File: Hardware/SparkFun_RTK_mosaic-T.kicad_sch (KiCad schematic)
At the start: 23 parts, among them J3 Qwiic_RA, U1 ESP32-WROVER-IE-N16R8

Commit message: More WIP
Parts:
- removed J3: Qwiic_RA, SparkFun-Connector:JST_SMD_1.0mm-4_RA, symbol SparkFun-Connector:Qwiic_Right_Angle
- added J7: Qwiic_Vertical, SparkFun-Connector:JST_SMD_1.0mm-4_Vertical, symbol SparkFun-Connector:Qwiic_Vertical
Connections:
- net 3.3V: now also J7.2 (Pin_2)
- net ESP21/SDA: now also J7.3 (Pin_3)
- net ESP22/SCL: now also J7.4 (Pin_4)
- net GND: now also J7.1 (Pin_1)
- new net: J7.NC1 (NC), J7.NC2 (NC)
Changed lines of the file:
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@@
+	)
+	(symbol
+		(lib_id "SparkFun-PowerSymbol:3.3V")
+		(at 222.25 36.83 0)
+		(unit 1)
+		(exclude_from_sim no)
+		(in_bom yes)
+		(on_board yes)
+		(dnp no)
+		(property "Reference" "#PWR0101"
+			(at 222.25 40.64 0)
+			(effects
+				(font
+					(size 1.27 1.27)
+				)
+				(hide yes)
+			)
+		)
+		(property "Value" "3.3V"
+			(at 222.25 33.274 0)
+			(effects
+				(font
+					(size 1.27 1.27)
+				)
+			)
+		)
+		(property "Footprint" ""
+			(at 222.25 36.83 0)
+			(effects
+				(font
+					(size 1.27 1.27)
+				)
+				(hide yes)
+			)
+		)
+		(property "Datasheet" ""
+			(at 222.25 36.83 0)
+			(effects
+				(font
+					(size 1.27 1.27)
+				)
+				(hide yes)
+			)
+		)
+		(property "Description" "Power symbol creates a global label with name \"3.3V\""
+			(at 222.25 36.83 0)
+			(effects
+				(font
+					(size 1.27 1.27)
+				)
+				(hide yes)
+			)
+		)
+		(pin "1"
+		)
+		(instances
+			(project "SparkFun_RTK_mosaic-T"
+				(path "/e3dd3ae4-244d-4cba-9cca-5d2abf83f29a"
+					(reference "#PWR0101")
+					(unit 1)
+				)
+			)
+		)
 	)
 	(symbol
@@
 	)
 	(symbol
-		(lib_id "SparkFun-Connector:Qwiic_Right_Angle")
-		(at 228.6 40.64 0)
-		(unit 1)
-		(exclude_from_sim no)
-		(in_bom yes)
-		(on_board yes)
-		(dnp no)
-		(fields_autoplaced yes)
-		(property "Reference" "J3"
-			(at 237.49 40.64 0)
-			(effects
-				(font
-					(size 1.27 1.27)
-				)
-				(justify left)
-			)
-		)
-		(property "Value" "Qwiic_RA"
-			(at 237.49 43.18 0)
-			(effects
-				(font
-					(size 1.27 1.27)
-				)
-				(justify left)
-			)
-		)
-		(property "Footprint" "SparkFun-Connector:JST_SMD_1.0mm-4_RA"
-			(at 228.6 53.34 0)
-			(effects
-				(font
-					(size 1.27 1.27)
-				)
-				(hide yes)
-			)
-		)
-		(property "Datasheet" "https://www.jst-mfg.com/product/pdf/eng/eSH.pdf"
-			(at 228.6 55.88 0)
-			(effects
-				(font
-					(size 1.27 1.27)
-				)
-				(hide yes)
-			)
-		)
-		(property "Description" "4 pin JST 1mm polarized connector for I2C"
-			(at 228.6 40.64 0)
-			(effects
-				(font
-					(size 1.27 1.27)
-				)
-				(hide yes)
-			)
-		)
-		(property "PROD_ID" "CONN-13694"
-			(at 228.6 50.8 0)
-			(effects
-				(font
-					(size 1.27 1.27)
-				)
-				(hide yes)
-			)
-		)
-		(pin "1"
-		)
-		(pin "2"
-		)
-		(pin "3"
-		)
-		(pin "4"
-		)
-		(pin "NC1"
-		)
-		(pin "NC2"
-		)
-		(instances
-			(project "SparkFun_RTK_Facet_mosaic"
-				(path "/e3dd3ae4-244d-4cba-9cca-5d2abf83f29a"
-					(reference "J3")
-					(unit 1)
-				)
-			)
-		)
-	)
-	(symbol
 		(lib_id "SparkFun-Aesthetic:SparkFun_Logo")
 		(at 213.36 182.88 0)
@@
 	)
 	(symbol
+		(lib_id "SparkFun-Connector:Qwiic_Vertical")
+		(at 228.6 40.64 0)
+		(unit 1)
+		(exclude_from_sim no)
+		(in_bom yes)
+		(on_board yes)
+		(dnp no)
+		(fields_autoplaced yes)
+		(property "Reference" "J7"
+			(at 237.49 40.6399 0)
+			(effects
+				(font
+					(size 1.27 1.27)
+				)
+				(justify left)
+			)
+		)
+		(property "Value" "Qwiic_Vertical"
+			(at 237.49 43.1799 0)
+			(effects
+				(font
+					(size 1.27 1.27)
+				)
+				(justify left)
+			)
+		)
+		(property "Footprint" "SparkFun-Connector:JST_SMD_1.0mm-4_Vertical"
+			(at 228.6 53.34 0)
+			(effects
+				(font
+					(size 1.27 1.27)
+				)
+				(hide yes)
+			)
+		)
+		(property "Datasheet" "https://www.jst-mfg.com/product/pdf/eng/eSH.pdf"
+			(at 228.6 55.88 0)
+			(effects
+				(font
+					(size 1.27 1.27)
+				)
+				(hide yes)
+			)
+		)
+		(property "Description" "4 pin JST 1mm polarized connector for I2C"
+			(at 228.6 40.64 0)
+			(effects
+				(font
+					(size 1.27 1.27)
+				)
+				(hide yes)
+			)
+		)
+		(property "PROD_ID" "CONN-14483"
+			(at 228.6 50.8 0)
+			(effects
+				(font
+					(size 1.27 1.27)
+				)
+				(hide yes)
+			)
+		)
+		(pin "3"
+		)
+		(pin "2"
+		)
+		(pin "4"
+		)
+		(pin "NC2"
+		)
+		(pin "NC1"
+		)
+		(pin "1"
+		)
+		(instances
+			(project ""
+				(path "/e3dd3ae4-244d-4cba-9cca-5d2abf83f29a"
+					(reference "J7")
+					(unit 1)
+				)
+			)
+		)
+	)
+	(symbol
 		(lib_id "SparkFun-PowerSymbol:3.3V")
 		(at 55.88 106.68 0)
@@
 					(unit 1)
 				)
-			)
-		)
-	)
-	(symbol
-		(lib_id "SparkFun-PowerSymbol:3.3V_P")
-		(at 222.25 36.83 0)
-		(unit 1)
-		(exclude_from_sim no)
-		(in_bom yes)
-		(on_board yes)
-		(dnp no)
-		(property "Reference" "#PWR0101"
-			(at 222.25 40.64 0)
-			(effects
-				(font
-					(size 1.27 1.27)
-				)
-				(hide yes)
-			)
-		)
-		(property "Value" "3.3V_P"
-			(at 222.25 33.274 0)
-			(effects
-				(font
-					(size 1.27 1.27)
-				)
-			)
-		)
-		(property "Footprint" ""
-			(at 222.25 36.83 0)
-			(effects
-				(font
-					(size 1.27 1.27)
-				)
-				(hide yes)
-			)
-		)
-		(property "Datasheet" ""
-			(at 222.25 36.83 0)
-			(effects
-				(font
-					(size 1.27 1.27)
-				)
-				(hide yes)
-			)
-		)
-		(property "Description" "Power symbol creates a global label with name \"3.3V_P\""
-			(at 222.25 36.83 0)
-			(effects
-				(font
-					(size 1.27 1.27)
-				)
-				(hide yes)
-			)
-		)
-		(pin "1"
-		)
-		(instances
-			(project "SparkFun_RTK_Facet_mosaic"
-				(path "/e3dd3ae4-244d-4cba-9cca-5d2abf83f29a"
-					(reference "#PWR0101")
-					(unit 1)
-				)

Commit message: More WIP
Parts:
- added D11, D12: CBI_LED_3mm_YGR, SparkFun-LED:CBI_LED_Triple_3mm_PTH, symbol SparkFun-LED:CBI_LED_Triple_3mm_PTH_YGR
- added D15: PESD0402, SparkFun-Capacitor:C_0402_1005Metric, symbol SparkFun-DiscreteSemi:D_TVS_0402
- added J3: U.FL, SparkFun-Connector:U.FL, symbol SparkFun-RF:U.FL
- added J8: RP-SMA_Edge, SparkFun-Connector:RP-SMA_Edge, symbol SparkFun-RF:RP-SMA_EdgeMount
- added J9: Screw_Cage_3.5mm-10, SparkFun-Connector:Screw_Cage_3.5mm-10, symbol SparkFun-Connector:Screw_Cage_3.5mm-10
- added R12, R13, R38, R39, R40, R42: 470, SparkFun-Resistor:R_0603_1608Metric, symbol SparkFun-Resistor:470_0603
- FID1, FID2, FID3, FID4: value Fiducial_0.5 -> Fiducial_0.5mm
- G5: footprint SparkFun-Aesthetic:SparkFun_Logo_8mm -> (none)
- renumbered TP5 to TP1
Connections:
- net 3.3V: now also R38.2
- net GND: now also D11.CATHODE_1, D11.CATHODE_2, D11.CATHODE_3, D12.CATHODE_1, D12.CATHODE_2, D12.CATHODE_3, D15.1 (A1), J3.2 (Ext), J8.2 (Ext), J9.8 (Pin_1)
- net ESP26/MCTS1: now reaches U1.11 (IOA26)
- net ESP27/MRTS1: now reaches U1.12 (IOA27)
- net ESP32/LED_ERROR: now reaches U1.8 (IOA32)
- net ESP32/LED_ERROR: now also R12.2
- net ESP33/LED_LOCK: now reaches U1.9 (IOA33)
- net ESP33/LED_LOCK: now also R13.2
- net ESP~{RST} renamed ESP_~{RST}
- new net: D11.ANODE_3, R38.1
- new net: D12.ANODE_1, R39.1
- new net: D12.ANODE_2, R40.1
- new net: D12.ANODE_3, R42.1
- new net: D11.ANODE_1, R12.1
- new net: D11.ANODE_2, R13.1
- new net 50Ohm: D15.2 (A2), J3.1 (In), J8.1 (In)
- new net DC_IN+: J9.10 (Pin_1)
- new net DC_IN-: J9.9 (Pin_1)
- new net LED_LOG: R42.2
- new net LED_PVT: R40.2
- new net LED_RTK: R39.2
- new net MCTS2_I: J9.7 (Pin_2)
- new net MEventA_I: J9.3 (Pin_3)
- new net MEventB_I: J9.2 (Pin_2)
- new net MPPS_O: J9.1 (Pin_1)
- new net MRTS2_O: J9.6 (Pin_4)
- new net MRX2_I: J9.4 (Pin_4)
- new net MTX2_O: J9.5 (Pin_3)
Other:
- added sheet Level_Shifting (Level_Shifting.kicad_sch)
- added sheet Oscillator (Oscillator.kicad_sch)
- note added: "ESP32 RF"
- note added: "I/O Connector"
- note added: "LEDs"
- note removed: "Connectors"

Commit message: More WIP
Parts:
- added TP24: PTH, SparkFun-Connector:1x01, symbol SparkFun-Connector:TestPoint_PTH
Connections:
- net ESP35/DeviceSense: now also TP24.1
- net ESP18/SDA2: now reaches U1.30 (IO18)
- net ESP19/SCL2: now reaches U1.31 (IO19)
- net 50Ohm: no longer names the net of D15.2 (A2), J3.1 (In), J8.1 (In)
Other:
- removed sheet Oscillator
- note added: "50Ohm"
- note added: "Qwiic I²C (for OLED)"
- note removed: "Qwiic I²C"
- moved on the sheet: D11, D12, D15, J3, J8, J9, R12, R13, R38, R39, R40, R42

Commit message: Schematic complete
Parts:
- removed R8: 4.7k, SparkFun-Resistor:R_0402_1005Metric, symbol SparkFun-Resistor:4.7k_0402
- added C53: 10uF, SparkFun-Capacitor:C_0402_1005Metric, symbol SparkFun-Capacitor:10uF_0402_6.3V_20%
- added C54: 0.1uF, SparkFun-Capacitor:C_0603_1608Metric, symbol SparkFun-Capacitor:0.1uF_0603_25V_20%
- added JP15: ~, SparkFun-Jumper:Jumper_2_NO, symbol SparkFun-Jumper:SolderJumper_2_Open
- added JP16, JP17, JP18, JP19, JP20, JP21: ~, SparkFun-Jumper:Jumper_2_NC_Trace, symbol SparkFun-Jumper:SolderJumper_2_Bridged
- added R8: 1k, SparkFun-Resistor:R_0402_1005Metric, symbol SparkFun-Resistor:1k_0402
- added TP25, TP26, TP41, TP42, TP43: PTH, SparkFun-Connector:1x01, symbol SparkFun-Connector:TestPoint_PTH
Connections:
- net ESP21/SDA: now also TP26.1
- net ESP22/SCL: now also TP25.1
- net ESP35/DeviceSense: now also R8.1
- net GND: now also C53.2, C54.2, R8.2
- net MCTS2_I: now also J9.4 (Pin_4), JP15.1 (A); no longer J9.7 (Pin_2)
- net MRTS2_O: now also J9.5 (Pin_3); no longer J9.6 (Pin_4)
- net MRX2_I: now also J9.7 (Pin_2); no longer J9.4 (Pin_4)
- net MTX2_O: now also J9.6 (Pin_4); no longer J9.5 (Pin_3)
- net at R38.1: now also JP18.1 (A); no longer D11.ANODE_3
- net at U1.37 (IO23): now also TP41.1
- net at U1.5 (IA39): now also TP43.1
- net at U1.6 (IA34): now also TP42.1
- net at R39.1: now also JP19.1 (A); no longer D12.ANODE_1
- net at R40.1: now also JP20.1 (A); no longer D12.ANODE_2
- net at D12.ANODE_3: now also JP21.2 (B); no longer R42.1
- net at R12.1: now also JP16.1 (A); no longer D11.ANODE_1
- net at R13.1: now also JP17.1 (A); no longer D11.ANODE_2
- new net: D12.ANODE_2, JP20.2 (B)
- new net: D12.ANODE_1, JP19.2 (B)
- new net: D11.ANODE_2, JP17.2 (B)
- new net: D11.ANODE_3, JP18.2 (B)
- new net: JP21.1 (A), R42.1
- new net: D11.ANODE_1, JP16.2 (B)
- new net VCCIO: C53.1, C54.1, JP15.2 (B)
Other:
- note added: "Close jumper to use CTS for VCCIO power output"
- note added: "Device Sense identifies oscillator type / model"
- moved on the sheet: C1, C2, D11, D12, J7, J9, JP1, R12, R13, R3, R38, R39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

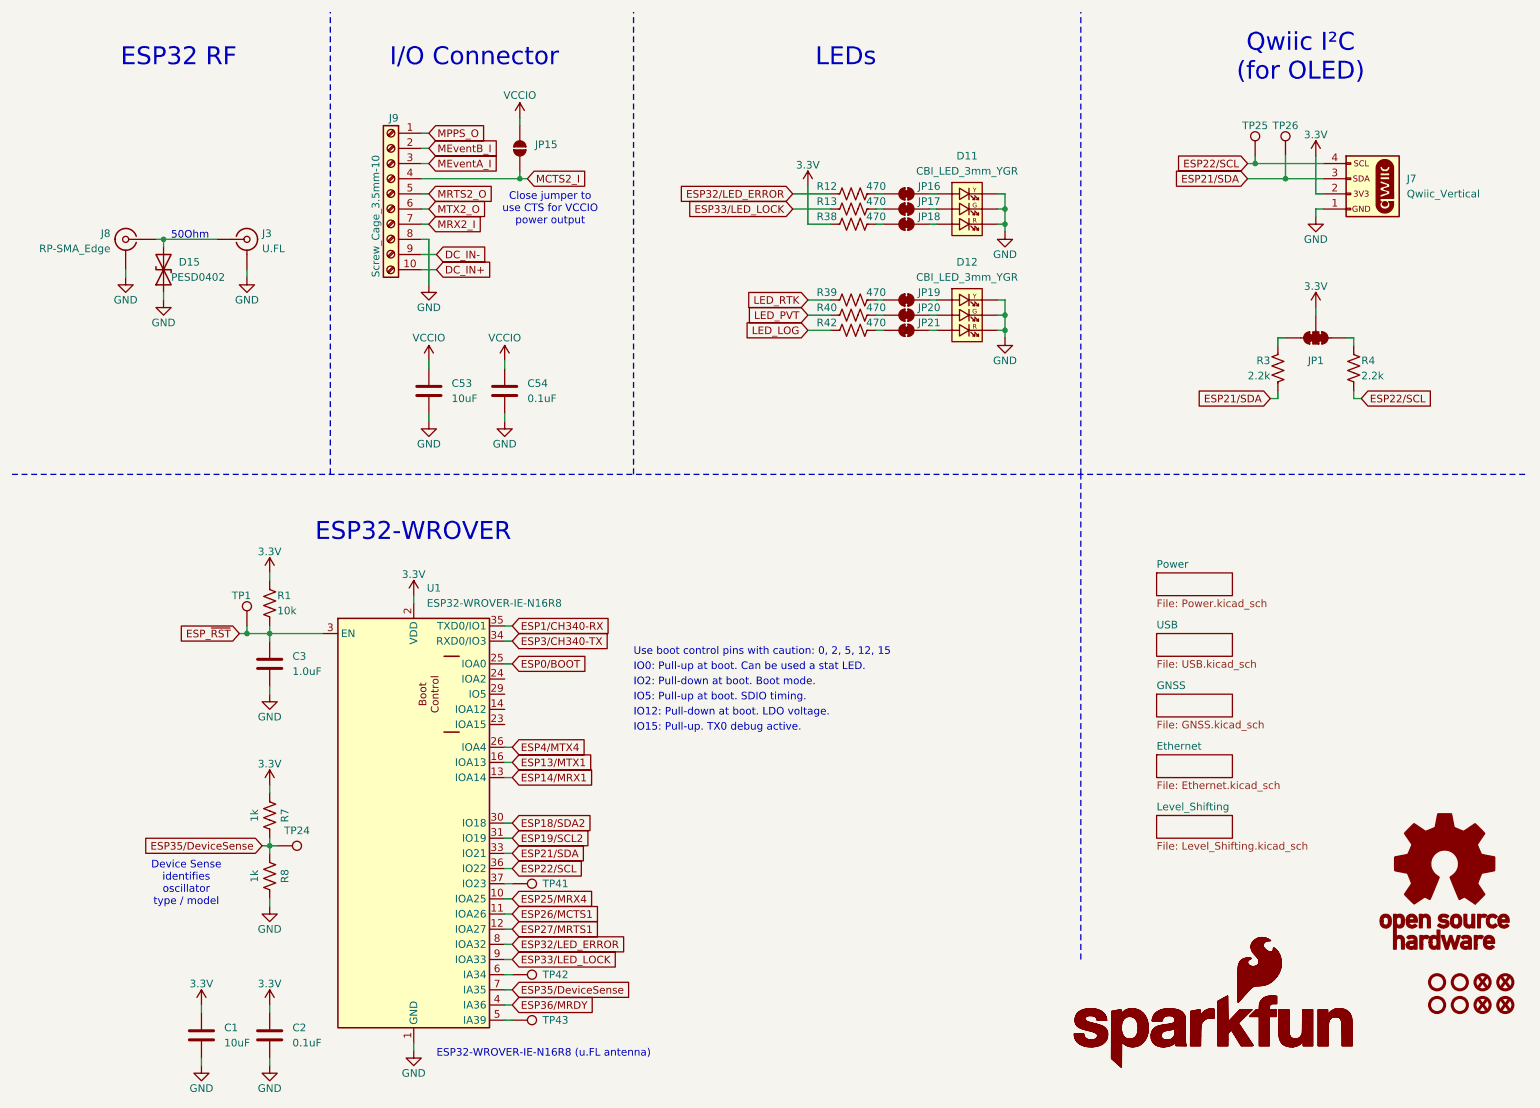
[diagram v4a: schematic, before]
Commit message: Ready for airwire review
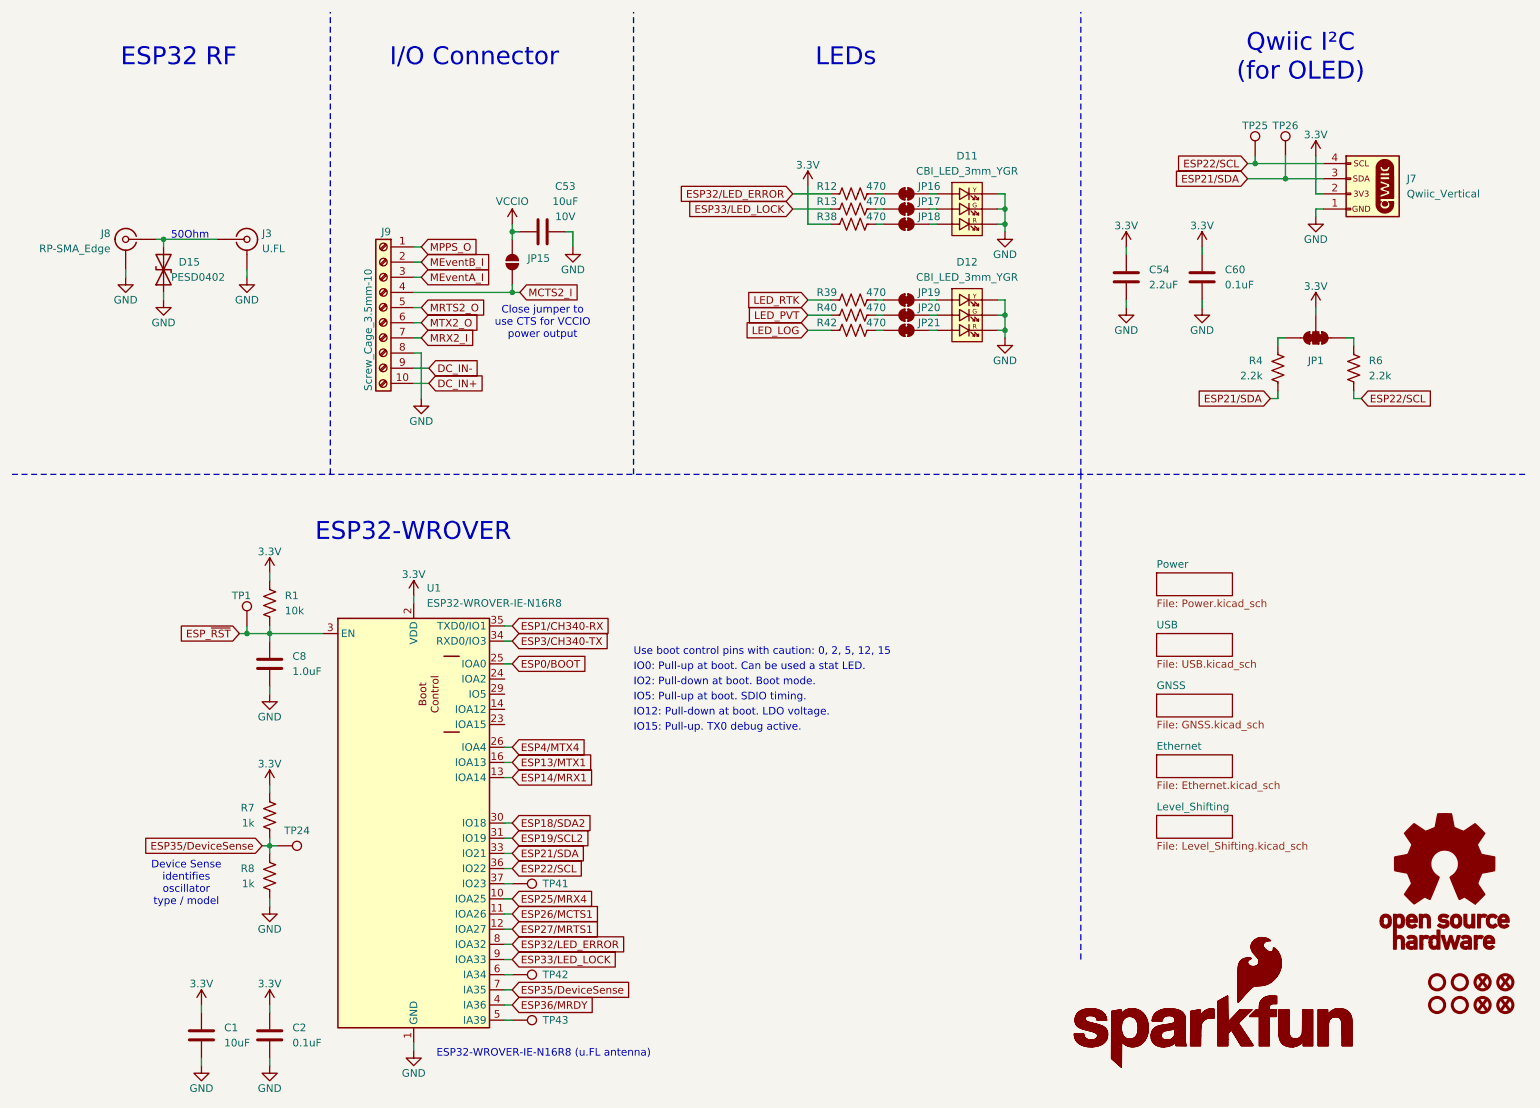
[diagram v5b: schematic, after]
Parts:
- removed C1, C53: 10uF, SparkFun-Capacitor:C_0402_1005Metric, symbol SparkFun-Capacitor:10uF_0402_6.3V_20%
- removed C2: 0.1uF, SparkFun-Capacitor:C_0402_1005Metric, symbol SparkFun-Capacitor:0.1uF_0402_6.3V_10%
- removed C3: 1.0uF, SparkFun-Capacitor:C_0402_1005Metric, symbol SparkFun-Capacitor:1.0uF_0402_16V_10%
- removed C54: 0.1uF, SparkFun-Capacitor:C_0603_1608Metric, symbol SparkFun-Capacitor:0.1uF_0603_25V_20%
- removed R1: 10k, SparkFun-Resistor:R_0402_1005Metric, symbol SparkFun-Resistor:10k_0402
- removed R3, R4: 2.2k, SparkFun-Resistor:R_0402_1005Metric, symbol SparkFun-Resistor:2.2k_0402
- removed R7, R8: 1k, SparkFun-Resistor:R_0402_1005Metric, symbol SparkFun-Resistor:1k_0402
- added C1: 10uF, SparkFun-Capacitor:C_0603_1608Metric, symbol SparkFun-Capacitor:10uF_0603_6.3V_20%
- added C2, C60: 0.1uF, SparkFun-Capacitor:C_0603_1608Metric, symbol SparkFun-Capacitor:0.1uF_0603_25V_20%
- added C53: 10uF, SparkFun-Capacitor:C_0603_1608Metric, symbol SparkFun-Capacitor:10uF_0603_10V_20%
- added C54: 2.2uF, SparkFun-Capacitor:C_0603_1608Metric, symbol SparkFun-Capacitor:2.2uF_0603_10V_20%
- added C8: 1.0uF, SparkFun-Capacitor:C_0603_1608Metric, symbol SparkFun-Capacitor:1.0uF_0603_16V_10%
- added R1: 10k, SparkFun-Resistor:R_0603_1608Metric, symbol SparkFun-Resistor:10k_0603
- added R4, R6: 2.2k, SparkFun-Resistor:R_0603_1608Metric, symbol SparkFun-Resistor:2.2k_0603
- added R7, R8: 1k, SparkFun-Resistor:R_0603_1608Metric, symbol SparkFun-Resistor:1k_0603
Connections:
- net 3.3V: now also C1.1, C2.1, C54.1, C60.1, R1.1, R7.1
- net ESP21/SDA: now also R4.1
- net ESP22/SCL: now also R6.1
- net ESP35/DeviceSense: now also R7.2, R8.1
- net ESP_~{RST}: now also C8.1, R1.2
- net GND: now also C1.2, C2.2, C53.2, C54.2, C60.2, C8.2, R8.2
- net VCCIO: now also C53.1
- net at JP1.1 (A): now also R6.2
- net at JP1.3 (B): now also R4.2
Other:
- moved on the sheet: J9, JP15
